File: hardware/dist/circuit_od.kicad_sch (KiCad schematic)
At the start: 26 parts, among them U5 TL072, U6 TL072

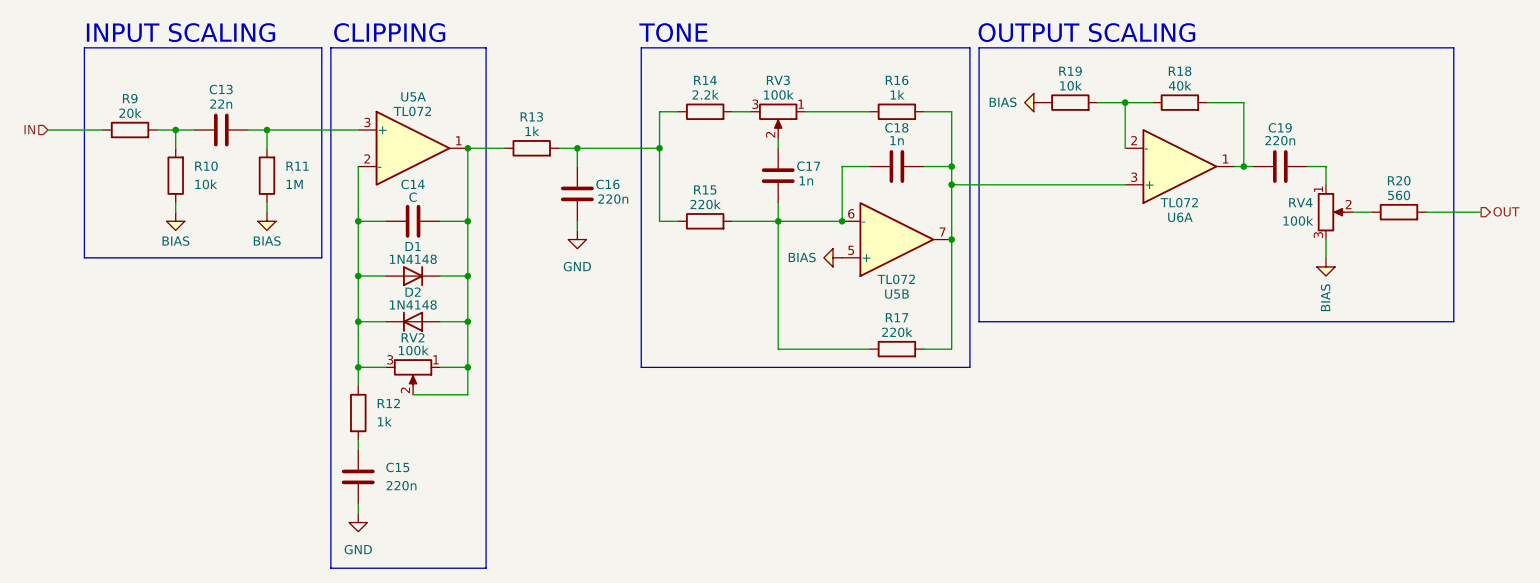
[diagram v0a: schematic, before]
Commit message: bom + kicad fix for dual supply
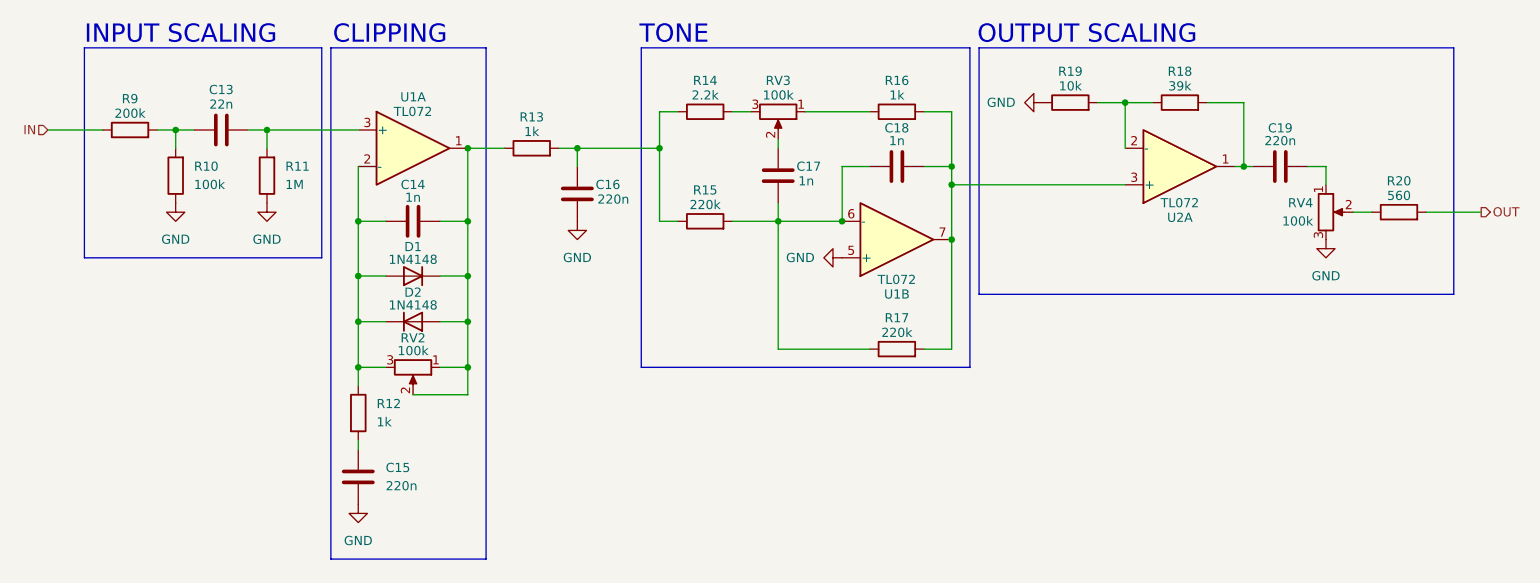
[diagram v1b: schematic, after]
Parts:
- C13, C15, C16, C17, C18, C19: footprint (none) -> Capacitor_SMD:C_0402_1005Metric
- C14: value C -> 1n; footprint (none) -> Capacitor_SMD:C_0402_1005Metric
- D1, D2: footprint Diode_THT:D_DO-35_SOD27_P7.62mm_Horizontal -> Diode_SMD:D_SOD-323
- R10: value 10k -> 100k; footprint (none) -> Resistor_SMD:R_0402_1005Metric
- R11, R12, R13, R14, R15, R16, R17, R19, R20: footprint (none) -> Resistor_SMD:R_0402_1005Metric
- R18: value 40k -> 39k; footprint (none) -> Resistor_SMD:R_0402_1005Metric
- R9: value 20k -> 200k; footprint (none) -> Resistor_SMD:R_0402_1005Metric
- RV2, RV3, RV4: footprint (none) -> Potentiometer_THT:Potentiometer_Alps_RK09K_Single_Vertical
- U1: renamed from U5; footprint (none) -> TL072CDT:D8_TEX_STM
- U2: renamed from U6; footprint (none) -> TL072CDT:D8_TEX_STM
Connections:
- net BIAS is gone; now on net GND: R10.1, R11.1, R19.1, RV4.3, U1.5 (+)

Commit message: finish pcb
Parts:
- C13, C14, C15, C16, C17, C18, C19: footprint Capacitor_SMD:C_0402_1005Metric -> Capacitor_SMD:C_0805_2012Metric_Pad1.18x1.45mm_HandSolder
- R10, R11, R12, R13, R14, R15, R16, R17, R18, R19, R20, R9: footprint Resistor_SMD:R_0402_1005Metric -> Resistor_SMD:R_0805_2012Metric_Pad1.20x1.40mm_HandSolder
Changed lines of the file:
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@@
 			)
 		)
-		(property "Footprint" "Resistor_SMD:R_0402_1005Metric"
+		(property "Footprint" "Resistor_SMD:R_0805_2012Metric_Pad1.20x1.40mm_HandSolder"
 			(at 142.24 102.108 90)
 			(hide yes)
@@
 			)
 		)
-		(property "Footprint" "Capacitor_SMD:C_0402_1005Metric"
+		(property "Footprint" "Capacitor_SMD:C_0805_2012Metric_Pad1.18x1.45mm_HandSolder"
 			(at 94.9452 139.7 0)
 			(hide yes)
@@
 			)
 		)
-		(property "Footprint" "Resistor_SMD:R_0402_1005Metric"
+		(property "Footprint" "Resistor_SMD:R_0805_2012Metric_Pad1.20x1.40mm_HandSolder"
 			(at 208.28 85.598 90)
 			(hide yes)
@@
 			)
 		)
-		(property "Footprint" "Resistor_SMD:R_0402_1005Metric"
+		(property "Footprint" "Resistor_SMD:R_0805_2012Metric_Pad1.20x1.40mm_HandSolder"
 			(at 62.23 89.408 90)
 			(hide yes)
@@
 			)
 		)
-		(property "Footprint" "Resistor_SMD:R_0402_1005Metric"
+		(property "Footprint" "Resistor_SMD:R_0805_2012Metric_Pad1.20x1.40mm_HandSolder"
 			(at 118.11 91.948 90)
 			(hide yes)
@@
 			)
 		)
-		(property "Footprint" "Resistor_SMD:R_0402_1005Metric"
+		(property "Footprint" "Resistor_SMD:R_0805_2012Metric_Pad1.20x1.40mm_HandSolder"
 			(at 70.358 93.98 90)
 			(hide yes)
@@
 			)
 		)
-		(property "Footprint" "Resistor_SMD:R_0402_1005Metric"
+		(property "Footprint" "Resistor_SMD:R_0805_2012Metric_Pad1.20x1.40mm_HandSolder"
 			(at 238.76 100.838 90)
 			(hide yes)
@@
 			)
 		)
-		(property "Footprint" "Resistor_SMD:R_0402_1005Metric"
+		(property "Footprint" "Resistor_SMD:R_0805_2012Metric_Pad1.20x1.40mm_HandSolder"
 			(at 168.91 86.868 90)
 			(hide yes)
@@
 			)
 		)
-		(property "Footprint" "Resistor_SMD:R_0402_1005Metric"
+		(property "Footprint" "Resistor_SMD:R_0805_2012Metric_Pad1.20x1.40mm_HandSolder"
 			(at 193.04 85.598 90)
 			(hide yes)
@@
 			)
 		)
-		(property "Footprint" "Resistor_SMD:R_0402_1005Metric"
+		(property "Footprint" "Resistor_SMD:R_0805_2012Metric_Pad1.20x1.40mm_HandSolder"
 			(at 92.202 127 90)
 			(hide yes)
@@
 			)
 		)
-		(property "Footprint" "Capacitor_SMD:C_0402_1005Metric"
+		(property "Footprint" "Capacitor_SMD:C_0805_2012Metric_Pad1.18x1.45mm_HandSolder"
 			(at 172.72 91.7448 0)
 			(hide yes)
@@
 			)
 		)
-		(property "Footprint" "Capacitor_SMD:C_0402_1005Metric"
+		(property "Footprint" "Capacitor_SMD:C_0805_2012Metric_Pad1.18x1.45mm_HandSolder"
 			(at 125.4252 100.33 0)
 			(hide yes)
@@
 			)
 		)
-		(property "Footprint" "Capacitor_SMD:C_0402_1005Metric"
+		(property "Footprint" "Capacitor_SMD:C_0805_2012Metric_Pad1.18x1.45mm_HandSolder"
 			(at 153.3652 97.79 0)
 			(hide yes)
@@
 			)
 		)
-		(property "Footprint" "Capacitor_SMD:C_0402_1005Metric"
+		(property "Footprint" "Capacitor_SMD:C_0805_2012Metric_Pad1.18x1.45mm_HandSolder"
 			(at 226.06 91.7448 0)
 			(hide yes)
@@
 			)
 		)
-		(property "Footprint" "Resistor_SMD:R_0402_1005Metric"
+		(property "Footprint" "Resistor_SMD:R_0805_2012Metric_Pad1.20x1.40mm_HandSolder"
 			(at 142.24 86.868 90)
 			(hide yes)
@@
 			)
 		)
-		(property "Footprint" "Resistor_SMD:R_0402_1005Metric"
+		(property "Footprint" "Resistor_SMD:R_0805_2012Metric_Pad1.20x1.40mm_HandSolder"
 			(at 83.058 93.98 90)
 			(hide yes)
@@
 			)
 		)
-		(property "Footprint" "Capacitor_SMD:C_0402_1005Metric"
+		(property "Footprint" "Capacitor_SMD:C_0805_2012Metric_Pad1.18x1.45mm_HandSolder"
 			(at 105.41 99.3648 0)
 			(hide yes)
@@
 			)
 		)
-		(property "Footprint" "Capacitor_SMD:C_0402_1005Metric"
+		(property "Footprint" "Capacitor_SMD:C_0805_2012Metric_Pad1.18x1.45mm_HandSolder"
 			(at 78.74 86.6648 0)
 			(hide yes)
@@
 			)
 		)
-		(property "Footprint" "Resistor_SMD:R_0402_1005Metric"
+		(property "Footprint" "Resistor_SMD:R_0805_2012Metric_Pad1.20x1.40mm_HandSolder"
 			(at 168.91 119.888 90)
 			(hide yes)
